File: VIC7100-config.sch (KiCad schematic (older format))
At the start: 31 parts, among them U13 VIC7100, U2 GD25LQ256DWIGR

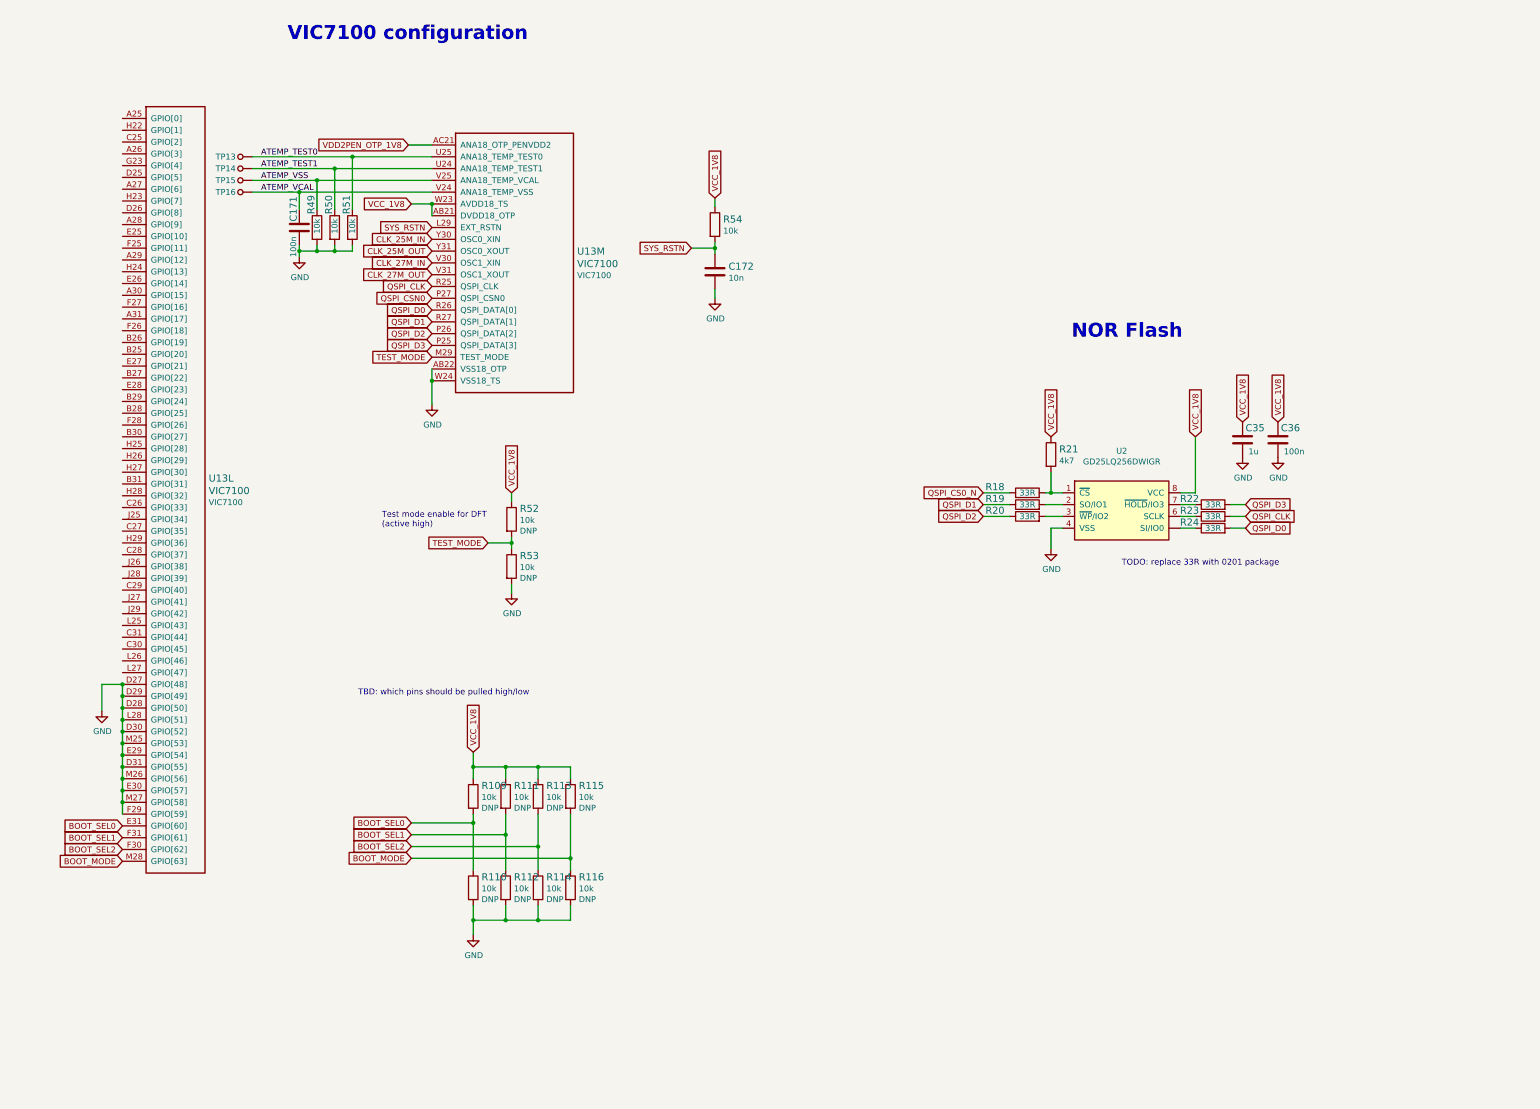
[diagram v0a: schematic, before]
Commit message: Updated VIC config, added reset and crystals
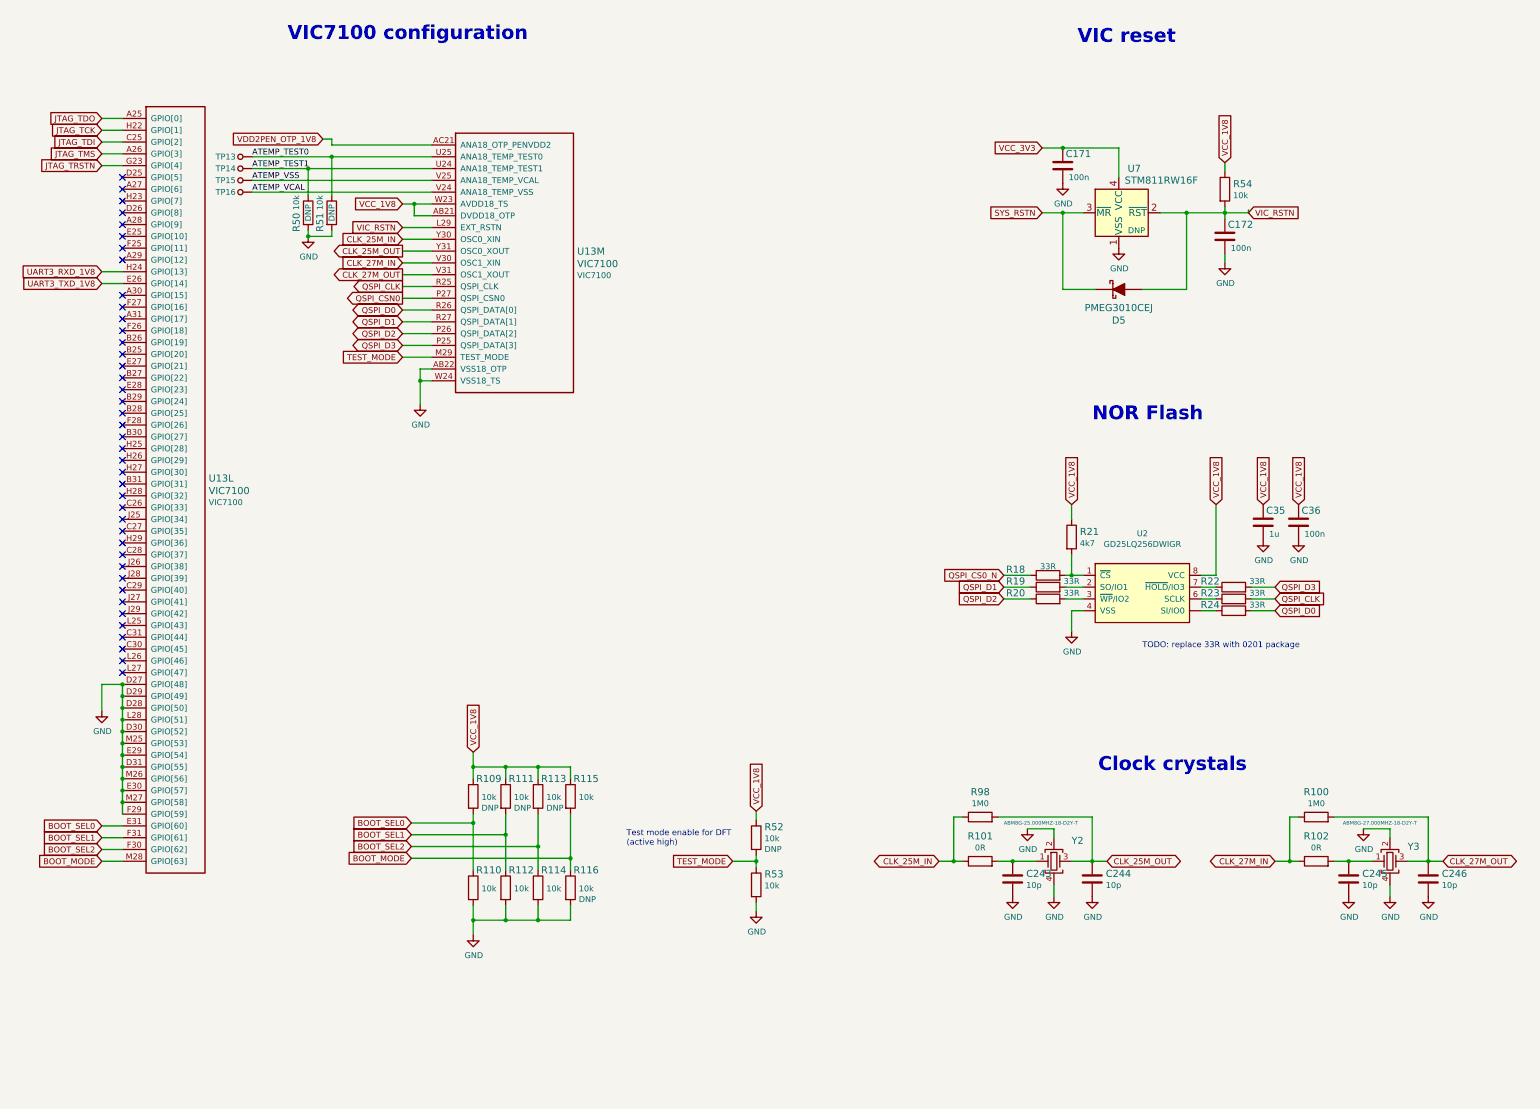
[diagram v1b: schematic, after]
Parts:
- removed C172: C_10n_0402, arvsom-footprints:0402-cap, symbol arvsom:C_10n_0402
- removed R49: R_10k_0402, arvsom-footprints:0402-res, symbol arvsom:R_10k_0402
- added C172: C_100n_0201, arvsom-footprints:0201-res, symbol arvsom:C_100n_0201
- added C243, C244, C245, C246: C_10p_0402, arvsom-footprints:0402-cap, symbol arvsom:C_10p_0402
- added D5: PMEG3010CEJ, arvsom-footprints:SOD-323F, symbol arvsom:PMEG3010CEJ
- added R100, R98: R_1M0_0402, arvsom-footprints:0402-res, symbol arvsom:R_1M0_0402
- added R101, R102: R_0R_0402, arvsom-footprints:0402-res, symbol arvsom:R_0R_0402
- added U7: STM811RW16F, arvsom-footprints:SOT-143-4, symbol arvsom:STM811RW16F
- added Y2: ABM8G-25.000MHZ-18-D2Y-T, arvsom-footprints:KX-7, symbol arvsom:ABM8G-25.000MHZ-18-D2Y-T
- added Y3: ABM8G-27.000MHZ-18-D2Y-T, arvsom-footprints:KX-7, symbol arvsom:ABM8G-27.000MHZ-18-D2Y-T
- R110, R112, R114, R115, R53: Populate DNP -> (none)
- R50, R51: DNP (none) -> DNP
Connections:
- net ATEMP_VCAL: no longer C171.1
- net CLK_25M_IN: now also R101.1, R98.1
- net CLK_25M_OUT: now also C244.1, R98.2, Y2.3
- net CLK_27M_IN: now also R100.1, R102.1
- net CLK_27M_OUT: now also C246.1, R100.2, Y3.3
- net GND: now also C172.2, C243.2, C244.2, C245.2, C246.2, U7.1 (VSS), Y2.2, Y2.4, Y3.2, Y3.4
- net SYS_RSTN: now also D5.K, U7.3 (~MR); no longer R54.2, U13.L29 (EXT_RSTN)
- net JTAG_TDO: now reaches U13.A25 (GPIO[0])
- net JTAG_TMS: now reaches U13.A26 (GPIO[3])
- net JTAG_TDI: now reaches U13.C25 (GPIO[2])
- net UART3_TXD_1V8: now reaches U13.E26 (GPIO[14])
- net JTAG_TRSTN: now reaches U13.G23 (GPIO[4])
- net JTAG_TCK: now reaches U13.H22 (GPIO[1])
- net UART3_RXD_1V8: now reaches U13.H24 (GPIO[13])
- new net: C243.1, R101.2, Y2.1
- new net: C245.1, R102.2, Y3.1
- new net VCC_3V3: C171.1, U7.4 (VCC)
- new net VIC_RSTN: C172.1, D5.A, R54.2, U13.L29 (EXT_RSTN), U7.2 (~RST)
- no-connect marks 0 -> 41
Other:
- note added: "Clock crystals"
- note added: "VIC reset"
- note removed: "TBD: which pins should be pulled high/low"
- moved on the sheet: C35, C36, R18, R19, R20, R21, R22, R23, R24, R50, R51, R52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

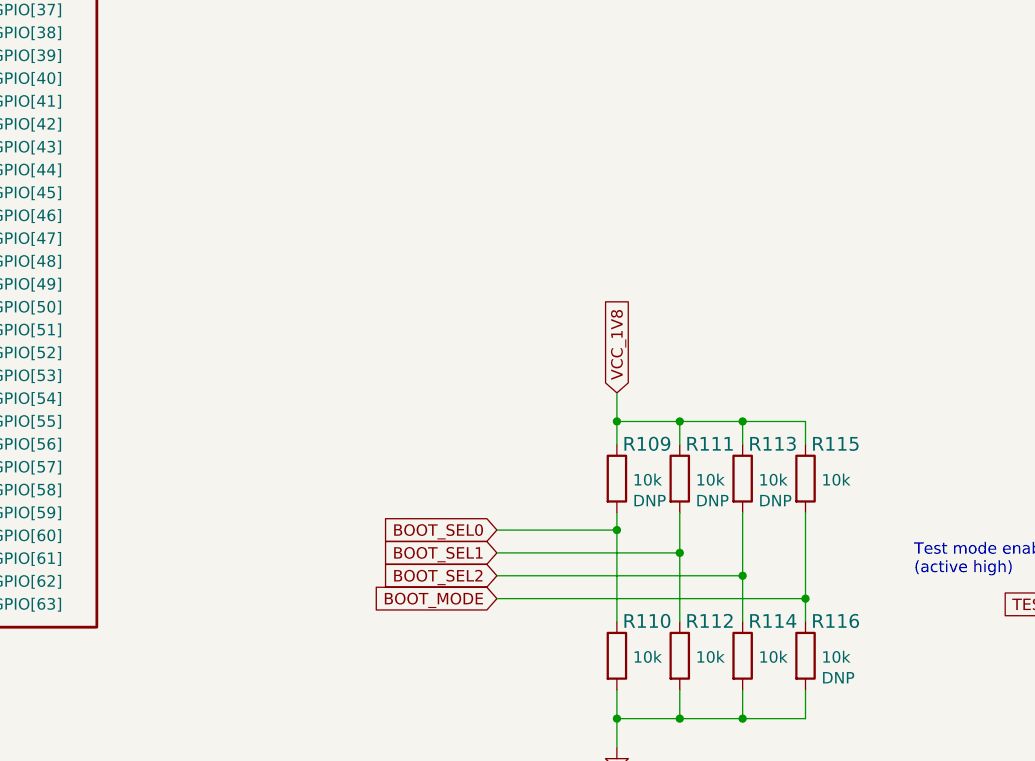
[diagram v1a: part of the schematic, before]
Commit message: Added BOOT_FROM_UART and power LED. Changed LED transistor to smaller footprint
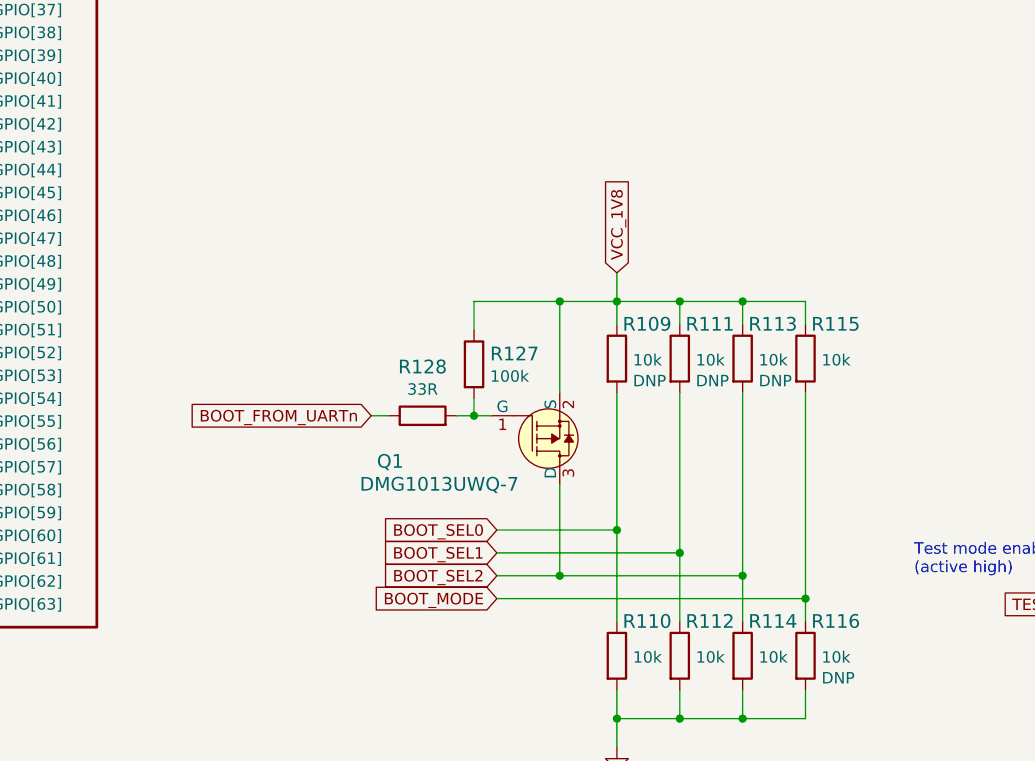
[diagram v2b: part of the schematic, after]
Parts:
- added Q1: DMG1013UWQ-7, arvsom-footprints:SOT-323, symbol arvsom:DMG1013UWQ-7
- added R127: R_100k_0402, arvsom-footprints:0402-res, symbol arvsom:R_100k_0402
- added R128: R_33R_0402, arvsom-footprints:0402-res, symbol arvsom:R_33R_0402
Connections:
- net BOOT_SEL2: now also Q1.3 (D)
- net VCC_1V8: now also Q1.2 (S), R127.1
- new net: Q1.1 (G), R127.2, R128.2
- new net BOOT_FROM_UARTn: R128.1
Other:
- moved on the sheet: R109, R111, R113, R115
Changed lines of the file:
@@
 	0    1    1    0
 $EndComp
-Text GLabel 5650 7625 1    50   Input ~ 0
+Text GLabel 5650 7100 1    50   Input ~ 0
 VCC_1V8
 $Comp
@@
 L arvsom:R_10k_0402 R109
 U 1 1 6280EA85
-P 5650 8000
-F 0 "R109" V 5500 8025 60  0000 L CNN
-F 1 "R_10k_0402" H 5650 7850 60  0001 C CNN
-F 2 "arvsom-footprints:0402-res" H 5850 8200 60  0001 L CNN
-F 3 "" H 5650 8000 50  0001 C CNN
-F 4 "VISHAY" H 5850 8400 60  0001 L CNN "Manufacturer"
-F 5 "CRCW040210K0FKEDHP" H 5850 8300 60  0001 L CNN "MPN"
-F 6 "10k" V 5657 8070 50  0000 L CNN "Val"
-F 7 "DNP" V 5748 8070 50  0000 L CNN "Populate"
-	1    5650 8000
+P 5650 7475
+F 0 "R109" V 5500 7500 60  0000 L CNN
+F 1 "R_10k_0402" H 5650 7325 60  0001 C CNN
+F 2 "arvsom-footprints:0402-res" H 5850 7675 60  0001 L CNN
+F 3 "" H 5650 7475 50  0001 C CNN
+F 4 "VISHAY" H 5850 7875 60  0001 L CNN "Manufacturer"
+F 5 "CRCW040210K0FKEDHP" H 5850 7775 60  0001 L CNN "MPN"
+F 6 "10k" V 5657 7545 50  0000 L CNN "Val"
+F 7 "DNP" V 5748 7545 50  0000 L CNN "Populate"
+	1    5650 7475
 	0    1    1    0
 $EndComp
@@
 	5125 8225 5650 8225
 Wire Wire Line
-	5650 8225 5650 8150
+	5650 8225 5650 7625
 Wire Wire Line
 	5125 8325 5925 8325
 Wire Wire Line
-	5925 8325 5925 8150
-Wire Wire Line
-	5125 8425 6200 8425
-Wire Wire Line
-	6200 8425 6200 8150
+	5925 8325 5925 7625
+Wire Wire Line
+	6200 8425 6200 7625
 Wire Wire Line
 	5125 8525 6475 8525
 Wire Wire Line
-	6475 8525 6475 8150
-Wire Wire Line
-	5650 7850 5650 7750
-Wire Wire Line
-	5925 7850 5925 7750
-Wire Wire Line
-	6200 7850 6200 7750
-Wire Wire Line
-	6475 7850 6475 7750
-Wire Wire Line
-	5650 7750 5925 7750
-Connection ~ 5925 7750
-Wire Wire Line
-	5925 7750 6200 7750
-Connection ~ 6200 7750
-Wire Wire Line
-	6200 7750 6475 7750
-Wire Wire Line
-	5650 7625 5650 7750
-Connection ~ 5650 7750
+	6475 8525 6475 7625
+Wire Wire Line
+	5650 7325 5650 7225
+Wire Wire Line
+	5925 7325 5925 7225
+Wire Wire Line
+	6200 7325 6200 7225
+Wire Wire Line
+	6475 7325 6475 7225
+Wire Wire Line
+	5650 7225 5925 7225
+Connection ~ 5925 7225
+Wire Wire Line
+	5925 7225 6200 7225
+Connection ~ 6200 7225
+Wire Wire Line
+	6200 7225 6475 7225
+Wire Wire Line
+	5650 7100 5650 7225
+Connection ~ 5650 7225
 Wire Wire Line
 	5650 8225 5650 8625
@@
 L arvsom:R_10k_0402 R111
 U 1 1 6295A918
-P 5925 8000
-F 0 "R111" V 5775 8025 60  0000 L CNN
-F 1 "R_10k_0402" H 5925 7850 60  0001 C CNN
-F 2 "arvsom-footprints:0402-res" H 6125 8200 60  0001 L CNN
-F 3 "" H 5925 8000 50  0001 C CNN
-F 4 "VISHAY" H 6125 8400 60  0001 L CNN "Manufacturer"
-F 5 "CRCW040210K0FKEDHP" H 6125 8300 60  0001 L CNN "MPN"
-F 6 "10k" V 5932 8070 50  0000 L CNN "Val"
-F 7 "DNP" V 6023 8070 50  0000 L CNN "Populate"
-	1    5925 8000
+P 5925 7475
+F 0 "R111" V 5775 7500 60  0000 L CNN
+F 1 "R_10k_0402" H 5925 7325 60  0001 C CNN
+F 2 "arvsom-footprints:0402-res" H 6125 7675 60  0001 L CNN
+F 3 "" H 5925 7475 50  0001 C CNN
+F 4 "VISHAY" H 6125 7875 60  0001 L CNN "Manufacturer"
+F 5 "CRCW040210K0FKEDHP" H 6125 7775 60  0001 L CNN "MPN"
+F 6 "10k" V 5932 7545 50  0000 L CNN "Val"
+F 7 "DNP" V 6023 7545 50  0000 L CNN "Populate"
+	1    5925 7475
 	0    1    1    0
 $EndComp
@@
 L arvsom:R_10k_0402 R113
 U 1 1 6295B1A5
-P 6200 8000
-F 0 "R113" V 6050 8025 60  0000 L CNN
-F 1 "R_10k_0402" H 6200 7850 60  0001 C CNN
-F 2 "arvsom-footprints:0402-res" H 6400 8200 60  0001 L CNN
-F 3 "" H 6200 8000 50  0001 C CNN
-F 4 "VISHAY" H 6400 8400 60  0001 L CNN "Manufacturer"
-F 5 "CRCW040210K0FKEDHP" H 6400 8300 60  0001 L CNN "MPN"
-F 6 "10k" V 6207 8070 50  0000 L CNN "Val"
-F 7 "DNP" V 6298 8070 50  0000 L CNN "Populate"
-	1    6200 8000
+P 6200 7475
+F 0 "R113" V 6050 7500 60  0000 L CNN
+F 1 "R_10k_0402" H 6200 7325 60  0001 C CNN
+F 2 "arvsom-footprints:0402-res" H 6400 7675 60  0001 L CNN
+F 3 "" H 6200 7475 50  0001 C CNN
+F 4 "VISHAY" H 6400 7875 60  0001 L CNN "Manufacturer"
+F 5 "CRCW040210K0FKEDHP" H 6400 7775 60  0001 L CNN "MPN"
+F 6 "10k" V 6207 7545 50  0000 L CNN "Val"
+F 7 "DNP" V 6298 7545 50  0000 L CNN "Populate"
+	1    6200 7475
 	0    1    1    0
 $EndComp
@@
 L arvsom:R_10k_0402 R115
 U 1 1 6295BA35
-P 6475 8000
-F 0 "R115" V 6325 8025 60  0000 L CNN
-F 1 "R_10k_0402" H 6475 7850 60  0001 C CNN
-F 2 "arvsom-footprints:0402-res" H 6675 8200 60  0001 L CNN
-F 3 "" H 6475 8000 50  0001 C CNN
-F 4 "VISHAY" H 6675 8400 60  0001 L CNN "Manufacturer"
-F 5 "CRCW040210K0FKEDHP" H 6675 8300 60  0001 L CNN "MPN"
-F 6 "10k" V 6482 8070 50  0000 L CNN "Val"
-	1    6475 8000
+P 6475 7475
+F 0 "R115" V 6325 7500 60  0000 L CNN
+F 1 "R_10k_0402" H 6475 7325 60  0001 C CNN
+F 2 "arvsom-footprints:0402-res" H 6675 7675 60  0001 L CNN
+F 3 "" H 6475 7475 50  0001 C CNN
+F 4 "VISHAY" H 6675 7875 60  0001 L CNN "Manufacturer"
+F 5 "CRCW040210K0FKEDHP" H 6675 7775 60  0001 L CNN "MPN"
+F 6 "10k" V 6482 7545 50  0000 L CNN "Val"
+	1    6475 7475
 	0    1    1    0
 $EndComp
@@
 Text Notes 10775 1625 0    118  ~ 24
 VIC reset
+$Comp
+L arvsom:R_33R_0402 R?
+U 1 1 60A536DD
+P 4800 7725
+AR Path="/60805CEC/60A536DD" Ref="R?"  Part="1"
+AR Path="/60805CC6/60A536DD" Ref="R128"  Part="1"
+F 0 "R128" H 4800 7938 60  0000 C CNN
+F 1 "R_33R_0402" H 4800 7575 60  0001 C CNN
+F 2 "arvsom-footprints:0402-res" H 5000 7925 60  0001 L CNN
+F 3 "" H 4800 7725 50  0001 C CNN
+F 4 "Vishay" H 5000 8125 60  0001 L CNN "Manufacturer"
+F 5 "CRCW040233R0FKED" H 5000 8025 60  0001 L CNN "MPN"
+F 6 "33R" H 4800 7840 50  0000 C CNN "Val"
+	1    4800 7725
+	1    0    0    -1
+$EndComp
+$Comp
+L arvsom:R_100k_0402 R?
+U 1 1 60A5BDE4
+P 5025 7500
+AR Path="/6293247C/60A5BDE4" Ref="R?"  Part="1"
+AR Path="/60805CC6/60A5BDE4" Ref="R127"  Part="1"
+F 0 "R127" V 4980 7570 60  0000 L CNN
+F 1 "R_100k_0402" H 5025 7350 60  0001 C CNN
+F 2 "arvsom-footprints:0402-res" H 5225 7700 60  0001 L CNN
+F 3 "" H 5025 7500 50  0001 C CNN
+F 4 "VISHAY" H 5225 7900 60  0001 L CNN "Manufacturer"
+F 5 "CRCW0402100KFKEDHP" H 5225 7800 60  0001 L CNN "MPN"
+F 6 "100k" V 5078 7570 50  0000 L CNN "Val"
+	1    5025 7500
+	0    1    1    0
+$EndComp
+$Comp
+L arvsom:DMG1013UWQ-7 Q1
+U 1 1 60A6338E
+P 5400 7825
+F 0 "Q1" H 4600 7925 60  0000 L CNN
+F 1 "DMG1013UWQ-7" H 4525 8025 60  0000 L CNN
+F 2 "arvsom-footprints:SOT-323" H 5600 8025 60  0001 L CNN
+F 3 "http://www.farnell.com/datasheets/2814383.pdf" H 5600 8125 60  0001 L CNN
+F 4 "DMG1013UWQ-7" H 5600 8325 60  0001 L CNN "MPN"
+F 5 "Diodes Incorporated" H 5600 8925 60  0001 L CNN "Manufacturer"
+	1    5400 7825
+	1    0    0    1
+$EndComp
+Wire Wire Line
+	5125 8425 5400 8425
+Wire Wire Line
+	5400 8025 5400 8425
+Connection ~ 5400 8425
+Wire Wire Line
+	5400 8425 6200 8425
+Wire Wire Line
+	5400 7625 5400 7225
+Wire Wire Line
+	5650 7225 5400 7225
+Wire Wire Line
+	5025 7225 5025 7350
+Connection ~ 5400 7225
+Wire Wire Line
+	5400 7225 5025 7225
+Wire Wire Line
+	5025 7650 5025 7725
+Wire Wire Line
+	4950 7725 5025 7725
+Connection ~ 5025 7725
+Wire Wire Line
+	5025 7725 5100 7725
+Text GLabel 4575 7725 0    50   Input ~ 0
+BOOT_FROM_UARTn
+Wire Wire Line
+	4575 7725 4650 7725
 $EndSCHEMATC
